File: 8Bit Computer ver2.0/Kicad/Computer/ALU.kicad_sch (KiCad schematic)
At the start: 36 parts, among them IC11 SN74HCS4075DR, IC12 SN74HCS4075DR, IC7 SN74LVC1G32DBVR, IC8 SN74LVC1G32DBVR

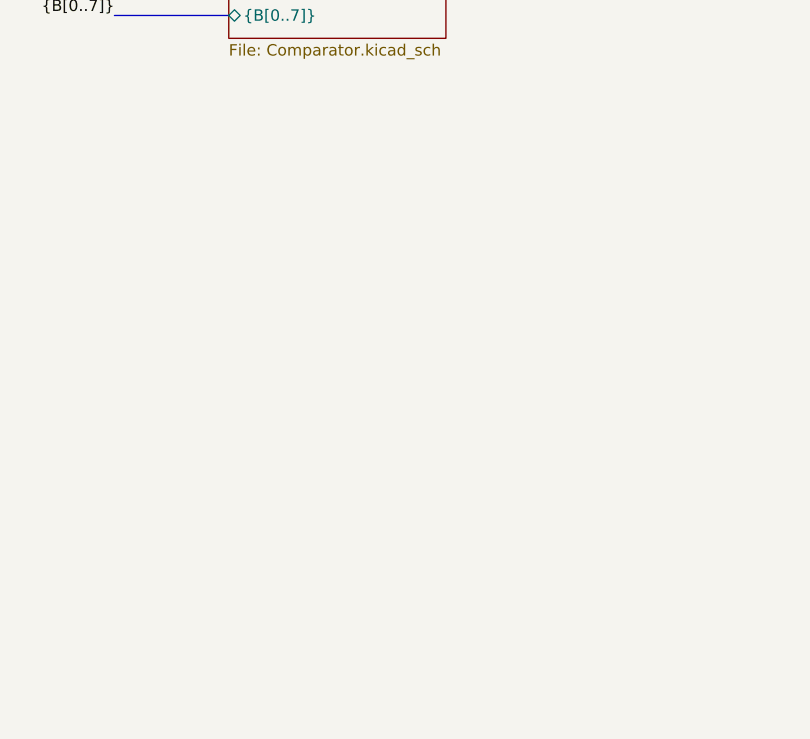
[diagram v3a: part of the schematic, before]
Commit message: parts, Kicad
parts:
added MUX 157 for BarrelShiftReg
Kicad:
began with BarrelShiftRegister
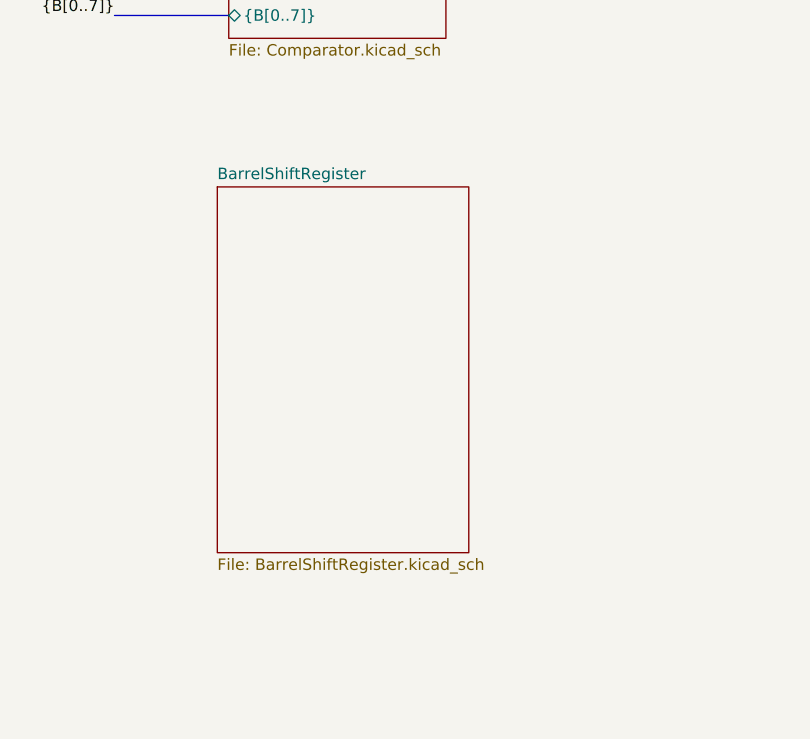
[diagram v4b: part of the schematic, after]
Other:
- added sheet BarrelShiftRegister (BarrelShiftRegister.kicad_sch)
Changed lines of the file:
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@@
+	)
+	(sheet
+		(at 466.09 354.33)
+		(size 27.94 40.64)
+		(exclude_from_sim no)
+		(in_bom yes)
+		(on_board yes)
+		(dnp no)
+		(fields_autoplaced yes)
+		(stroke
+			(width 0.1524)
+			(type solid)
+		)
+		(fill
+			(color 0 0 0 0.0000)
+		)
+		(property "Sheetname" "BarrelShiftRegister"
+			(at 466.09 353.6184 0)
+			(effects
+				(font
+					(size 1.27 1.27)
+				)
+				(justify left bottom)
+			)
+		)
+		(property "Sheetfile" "BarrelShiftRegister.kicad_sch"
+			(at 466.09 395.5546 0)
+			(effects
+				(font
+					(size 1.27 1.27)
+				)
+				(justify left top)
+			)
+		)
+		(instances
+			(project "Computer"
+				(path "/1196a00e-6878-4d6d-82b7-9e052dfe7c14/c4d8b530-1c6d-45af-88d2-7dc1d4321a34"
+					(page "15")
+				)
+			)
+		)
 	)
 	(sheet

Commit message: partsList, Kicad
parts:
added faster Comparator 521
added 1CH XOR
added 8Bit and 16Bit Driver 245, 16245
->they need pullUp resistors for High-Z when power on
Kicad:
included SRAM CAD Model AS7C1024
included some CAD Models
added Register 1 0x20 and 0x21
finished Incrementor
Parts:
- added C33, C34, C35, C36, C37, C38, C39, C40, C41, C42, C43, C44, C45, C46, C47, C48, C49, C50, C51, C52, C53, C54, C55, C56, C57, C58, C59, C60, C61, C62, C63, C64, C65, C66, C67, C68, C69, C70, C71, C72, C73, C74, C75, C76, C77, C78, C79, C80, C81, C82, C83, C84, C85, C86, C87, C88, C89, C90, C91, C92, C93, C94, C95, C96: 100nF, Capacitor_SMD:C_1206_3216Metric_Pad1.33x1.80mm_HandSolder, symbol Device:C
- added IC85: SN74ABT245BDWR, Samacsys:SOIC127P1030X265-20N, symbol Samacsys:SN74ABT245BDWR
- added IC86: SN74ABT574ADWR, Samacsys:SOIC127P1030X265-20N, symbol Samacsys:SN74ABT574ADWR
- added IC89: SN74LVC1G08DBVR, Samacsys:SOT95P280X145-5N, symbol Samacsys:SN74LVC1G08DBVR
- added IC90: SN74AHC74DR, Samacsys:SOIC127P600X175-14N, symbol Samacsys:SN74AHC74DR
- added IC91, IC94, IC95: SN74LVC1G14DBVR, Samacsys:SOT95P280X145-5N, symbol Samacsys:SN74LVC1G14DBVR
- added IC92, IC93: SN74F521DWR, Samacsys:SOIC127P1030X265-20N, symbol Samacsys:SN74F521DWR
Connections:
- net A0: now also IC85.2 (A1), IC86.19 (1Q)
- net A1: now also IC85.3 (A2), IC86.18 (2Q)
- net A2: now also IC85.4 (A3), IC86.17 (3Q)
- net A3: now also IC85.5 (A4), IC86.16 (4Q)
- net A4: now also IC85.6 (A5), IC86.15 (5Q)
- net A5: now also IC85.7 (A6), IC86.14 (6Q)
- net A6: now also IC85.8 (A7), IC86.13 (7Q)
- net A7: now also IC85.9 (A8), IC86.12 (8Q)
- net GND: now also C33.1, C34.1, C35.1, C36.1, C37.1, C38.1, C39.1, C40.1, C41.1, C42.1, C43.1, C44.1, C45.1, C46.1, C47.1, C48.1, C49.1, C50.1, C51.1, C52.1, C53.1, C54.1, C55.1, C56.1, C57.1, C58.1, C59.1, C60.1, C61.1, C62.1, C63.1, C64.1, C65.1, C66.1, C67.1, C68.1, C69.1, C70.1, C71.1, C72.1, C73.1, C74.1, C75.1, C76.1, C77.1, C78.1, C79.1, C80.1, C81.1, C82.1, C83.1, C84.1, C85.1, C86.1, C87.1, C88.1, C89.1, C90.1, C91.1, C92.1, C93.1, C94.1, C95.1, C96.1, IC85.10 (GND), IC86.1 (~{OE}), IC86.10 (GND), IC89.3 (GND), IC90.7 (GND), IC91.3 (GND), IC92.1 (~{OE}), IC92.10 (GND), IC93.1 (~{OE}), IC93.10 (GND), IC94.3 (GND), IC95.3 (GND)
- net VCC: now also C33.2, C34.2, C35.2, C36.2, C37.2, C38.2, C39.2, C40.2, C41.2, C42.2, C43.2, C44.2, C45.2, C46.2, C47.2, C48.2, C49.2, C50.2, C51.2, C52.2, C53.2, C54.2, C55.2, C56.2, C57.2, C58.2, C59.2, C60.2, C61.2, C62.2, C63.2, C64.2, C65.2, C66.2, C67.2, C68.2, C69.2, C70.2, C71.2, C72.2, C73.2, C74.2, C75.2, C76.2, C77.2, C78.2, C79.2, C80.2, C81.2, C82.2, C83.2, C84.2, C85.2, C86.2, C87.2, C88.2, C89.2, C90.2, C91.2, C92.2, C93.2, C94.2, C95.2, C96.2, IC85.1 (DIR), IC85.20 (VCC), IC86.20 (VCC), IC89.5 (VCC), IC90.1 (1~{CLR}), IC90.10 (2~{PRE}), IC90.11 (2CLK), IC90.12 (2D), IC90.13 (2~{CLR}), IC90.14 (VCC), IC90.4 (1~{PRE}), IC91.5 (VCC), IC92.20 (VCC), IC93.20 (VCC), IC94.5 (VCC), IC95.5 (VCC)
- net ~{CLK}: now also IC89.2 (B), IC91.2 (A)
- new net: IC92.19 (~{P_=_Q}), IC95.2 (A)
- new net: IC89.1 (A), IC95.4 (Y)
- new net: IC86.11 (CLK), IC89.4 (Y)
- new net: IC90.2 (1D), IC94.4 (Y)
- new net: IC90.3 (1CLK), IC91.4 (Y)
- new net: IC85.19 (~{OE}), IC90.6 (1~{Q})
- new net: IC93.19 (~{P_=_Q}), IC94.2 (A)
- new net CMD0: IC92.2 (P0), IC93.2 (P0)
- new net CMD1: IC92.4 (P1), IC93.4 (P1)
- new net CMD2: IC92.6 (P2), IC93.6 (P2)
- new net CMD3: IC92.8 (P3), IC93.8 (P3)
- new net CMD4: IC92.11 (P4), IC93.11 (P4)
- new net CMD5: IC92.13 (P5), IC93.13 (P5)
- new net CMD6: IC92.15 (P6), IC93.15 (P6)
- new net CMD7: IC92.17 (P7), IC93.17 (P7)
- new net DAT0: IC86.2 (1D)
- new net DAT1: IC86.3 (2D)
- new net DAT2: IC86.4 (3D)
- new net DAT3: IC86.5 (4D)
- new net DAT4: IC86.6 (5D)
- new net DAT5: IC86.7 (6D)
- new net DAT6: IC86.8 (7D)
- new net DAT7: IC86.9 (8D)
- new net Q0: IC85.18 (B1)
- new net Q1: IC85.17 (B2)
- new net Q2: IC85.16 (B3)
- new net Q3: IC85.15 (B4)
- new net Q4: IC85.14 (B5)
- new net Q5: IC85.13 (B6)
- new net Q6: IC85.12 (B7)
- new net Q7: IC85.11 (B8)
- no-connect marks 0 -> 3
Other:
- sheet BarrelShiftRegister ports: added DIS[0..7], GND, Q, STC, STF, VCC, {A[0..7]}, ~{CLK}; removed none
- sheet Incrementor ports: added Q[0..7], {C[0..7]}; removed C, Q
- note added: "0x20"
- note added: "0x21"
- note added: "REGISTER1"

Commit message: Kicad
added Register 2(0x22 u 0x23) and 3(0x13 u 0x14)
added BarrelShiftRegister
added AdderSubstractor
added cmd Comparators to the bitwise and binary Logic
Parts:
- added C100, C101, C102, C103, C104, C105, C106, C107, C108, C109, C110, C111, C112, C113, C114, C115, C116, C117, C118, C119, C120, C97, C98, C99: 100nF, Capacitor_SMD:C_1206_3216Metric_Pad1.33x1.80mm_HandSolder, symbol Device:C
- added IC100, IC107, IC108, IC109, IC125, IC126, IC128, IC130, IC132, IC134, IC136, IC138, IC98, IC99: SN74LVC1G14DBVR, Samacsys:SOT95P280X145-5N, symbol Samacsys:SN74LVC1G14DBVR
- added IC101, IC110: SN74ABT574ADWR, Samacsys:SOIC127P1030X265-20N, symbol Samacsys:SN74ABT574ADWR
- added IC102, IC111: SN74AHC74DR, Samacsys:SOIC127P600X175-14N, symbol Samacsys:SN74AHC74DR
- added IC103, IC112: SN74LVC1G08DBVR, Samacsys:SOT95P280X145-5N, symbol Samacsys:SN74LVC1G08DBVR
- added IC104, IC113: SN74ABT245BDWR, Samacsys:SOIC127P1030X265-20N, symbol Samacsys:SN74ABT245BDWR
- added IC105, IC106, IC123, IC124, IC127, IC129, IC131, IC133, IC135, IC137, IC96, IC97: SN74F521DWR, Samacsys:SOIC127P1030X265-20N, symbol Samacsys:SN74F521DWR
- added IC114: SN74LVC1G32DBVR, Samacsys:SOT95P280X145-5N, symbol Samacsys:SN74LVC1G32DBVR
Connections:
- net B0: now also IC101.19 (1Q), IC104.2 (A1)
- net B1: now also IC101.18 (2Q), IC104.3 (A2)
- net B2: now also IC101.17 (3Q), IC104.4 (A3)
- net B3: now also IC101.16 (4Q), IC104.5 (A4)
- net B4: now also IC101.15 (5Q), IC104.6 (A5)
- net B5: now also IC101.14 (6Q), IC104.7 (A6)
- net B6: now also IC101.13 (7Q), IC104.8 (A7)
- net B7: now also IC101.12 (8Q), IC104.9 (A8)
- net BinaryAND/EN: now also IC128.4 (Y)
- net BinaryNOT/EN: now also IC132.4 (Y)
- net BinaryOR/EN: now also IC130.4 (Y)
- net BinaryXOR/EN: now also IC125.4 (Y)
- net BitwiseAND/EN: now also IC136.4 (Y)
- net BitwiseNOT/EN: now also IC126.4 (Y)
- net BitwiseOR/EN: now also IC134.4 (Y)
- net BitwiseXOR/EN: now also IC138.4 (Y)
- net CMD0: now also IC105.2 (P0), IC106.2 (P0), IC123.2 (P0), IC124.2 (P0), IC127.2 (P0), IC129.2 (P0), IC131.2 (P0), IC133.2 (P0), IC135.2 (P0), IC137.2 (P0), IC96.2 (P0), IC97.2 (P0)
- net CMD1: now also IC105.4 (P1), IC106.4 (P1), IC123.4 (P1), IC124.4 (P1), IC127.4 (P1), IC129.4 (P1), IC131.4 (P1), IC133.4 (P1), IC135.4 (P1), IC137.4 (P1), IC96.4 (P1), IC97.4 (P1)
- net CMD2: now also IC105.6 (P2), IC106.6 (P2), IC123.6 (P2), IC124.6 (P2), IC127.6 (P2), IC129.6 (P2), IC131.6 (P2), IC133.6 (P2), IC135.6 (P2), IC137.6 (P2), IC96.6 (P2), IC97.6 (P2)
- net CMD3: now also IC105.8 (P3), IC106.8 (P3), IC123.8 (P3), IC124.8 (P3), IC127.8 (P3), IC129.8 (P3), IC131.8 (P3), IC133.8 (P3), IC135.8 (P3), IC137.8 (P3), IC96.8 (P3), IC97.8 (P3)
- net CMD4: now also IC105.11 (P4), IC106.11 (P4), IC123.11 (P4), IC124.11 (P4), IC127.11 (P4), IC129.11 (P4), IC131.11 (P4), IC133.11 (P4), IC135.11 (P4), IC137.11 (P4), IC96.11 (P4), IC97.11 (P4)
- net CMD5: now also IC105.13 (P5), IC106.13 (P5), IC123.13 (P5), IC124.13 (P5), IC127.13 (P5), IC129.13 (P5), IC131.13 (P5), IC133.13 (P5), IC135.13 (P5), IC137.13 (P5), IC96.13 (P5), IC97.13 (P5)
- net CMD6: now also IC105.15 (P6), IC106.15 (P6), IC123.15 (P6), IC124.15 (P6), IC127.15 (P6), IC129.15 (P6), IC131.15 (P6), IC133.15 (P6), IC135.15 (P6), IC137.15 (P6), IC96.15 (P6), IC97.15 (P6)
- net CMD7: now also IC105.17 (P7), IC106.17 (P7), IC123.17 (P7), IC124.17 (P7), IC127.17 (P7), IC129.17 (P7), IC131.17 (P7), IC133.17 (P7), IC135.17 (P7), IC137.17 (P7), IC96.17 (P7), IC97.17 (P7)
- net DAT0: now also IC101.2 (1D), IC110.2 (1D)
- net DAT1: now also IC101.3 (2D), IC110.3 (2D)
- net DAT2: now also IC101.4 (3D), IC110.4 (3D)
- net DAT3: now also IC101.5 (4D), IC110.5 (4D)
- net DAT4: now also IC101.6 (5D), IC110.6 (5D)
- net DAT5: now also IC101.7 (6D), IC110.7 (6D)
- net DAT6: now also IC101.8 (7D), IC110.8 (7D)
- net DAT7: now also IC101.9 (8D), IC110.9 (8D)
- net GND: now also IC92.12 (Q4), IC92.16 (Q6), IC92.18 (Q7), IC92.3 (Q0), IC92.5 (Q1), IC92.7 (Q2), IC92.9 (Q3), IC93.12 (Q4), IC93.16 (Q6), IC93.18 (Q7), IC93.5 (Q1), IC93.7 (Q2), IC93.9 (Q3), C100.1, C101.1, C102.1, C103.1, C104.1, C105.1, C106.1, C107.1, C108.1, C109.1, C110.1, C111.1, C112.1, C113.1, C114.1, C115.1, C116.1, C117.1, C118.1, C119.1, C120.1, C97.1, C98.1, C99.1, IC100.3 (GND), IC101.1 (~{OE}), IC101.10 (GND), IC102.7 (GND), IC103.3 (GND), IC104.10 (GND), IC105.1 (~{OE}), IC105.10 (GND), IC105.14 (Q5), IC105.16 (Q6), IC105.18 (Q7), IC105.7 (Q2), IC105.9 (Q3), IC106.1 (~{OE}), IC106.10 (GND), IC106.14 (Q5), IC106.16 (Q6), IC106.18 (Q7), IC106.3 (Q0), IC106.5 (Q1), IC106.9 (Q3), IC107.3 (GND), IC108.3 (GND), IC109.3 (GND), IC110.1 (~{OE}), IC110.10 (GND), IC111.7 (GND), IC112.3 (GND), IC113.10 (GND), IC114.3 (GND), IC123.1 (~{OE}), IC123.10 (GND), IC123.14 (Q5), IC123.16 (Q6), IC123.18 (Q7), IC123.3 (Q0), IC123.5 (Q1), IC123.7 (Q2), IC124.1 (~{OE}), IC124.10 (GND), IC124.14 (Q5), IC124.16 (Q6), IC124.18 (Q7), IC124.5 (Q1), IC124.7 (Q2), IC125.3 (GND), IC126.3 (GND), IC127.1 (~{OE}), IC127.10 (GND), IC127.14 (Q5), IC127.16 (Q6), IC127.18 (Q7), IC127.9 (Q3), IC128.3 (GND), IC129.1 (~{OE}), IC129.10 (GND), IC129.14 (Q5), IC129.16 (Q6), IC129.18 (Q7), IC129.3 (Q0), IC129.9 (Q3), IC130.3 (GND), IC131.1 (~{OE}), IC131.10 (GND), IC131.14 (Q5), IC131.16 (Q6), IC131.18 (Q7), IC131.5 (Q1), IC131.9 (Q3), IC132.3 (GND), IC133.1 (~{OE}), IC133.10 (GND), IC133.14 (Q5), IC133.16 (Q6), IC133.18 (Q7), IC133.3 (Q0), IC133.7 (Q2), IC134.3 (GND), IC135.1 (~{OE}), IC135.10 (GND), IC135.14 (Q5), IC135.16 (Q6), IC135.18 (Q7), IC135.7 (Q2), IC136.3 (GND), IC137.1 (~{OE}), IC137.10 (GND), IC137.14 (Q5), IC137.16 (Q6), IC137.18 (Q7), IC137.3 (Q0), IC137.5 (Q1), IC138.3 (GND), IC96.1 (~{OE}), IC96.10 (GND), IC96.12 (Q4), IC96.16 (Q6), IC96.18 (Q7), IC96.3 (Q0), IC96.7 (Q2), IC96.9 (Q3), IC97.1 (~{OE}), IC97.10 (GND), IC97.12 (Q4), IC97.16 (Q6), IC97.18 (Q7), IC97.7 (Q2), IC97.9 (Q3), IC98.3 (GND), IC99.3 (GND)
- net Q0: now also IC104.18 (B1), IC113.18 (B1)
- net Q1: now also IC104.17 (B2), IC113.17 (B2)
- net Q2: now also IC104.16 (B3), IC113.16 (B3)
- net Q3: now also IC104.15 (B4), IC113.15 (B4)
- net Q4: now also IC104.14 (B5), IC113.14 (B5)
- net Q5: now also IC104.13 (B6), IC113.13 (B6)
- net Q6: now also IC104.12 (B7), IC113.12 (B7)
- net Q7: now also IC104.11 (B8), IC113.11 (B8)
- net VCC: now also IC92.14 (Q5), IC93.14 (Q5), IC93.3 (Q0), C100.2, C101.2, C102.2, C103.2, C104.2, C105.2, C106.2, C107.2, C108.2, C109.2, C110.2, C111.2, C112.2, C113.2, C114.2, C115.2, C116.2, C117.2, C118.2, C119.2, C120.2, C97.2, C98.2, C99.2, IC100.5 (VCC), IC101.20 (VCC), IC102.1 (1~{CLR}), IC102.10 (2~{PRE}), IC102.11 (2CLK), IC102.12 (2D), IC102.13 (2~{CLR}), IC102.14 (VCC), IC102.4 (1~{PRE}), IC103.5 (VCC), IC104.1 (DIR), IC104.20 (VCC), IC105.12 (Q4), IC105.20 (VCC), IC105.3 (Q0), IC105.5 (Q1), IC106.12 (Q4), IC106.20 (VCC), IC106.7 (Q2), IC107.5 (VCC), IC108.5 (VCC), IC109.5 (VCC), IC110.20 (VCC), IC111.1 (1~{CLR}), IC111.10 (2~{PRE}), IC111.11 (2CLK), IC111.12 (2D), IC111.13 (2~{CLR}), IC111.14 (VCC), IC111.4 (1~{PRE}), IC112.5 (VCC), IC113.1 (DIR), IC113.20 (VCC), IC114.5 (VCC), IC123.12 (Q4), IC123.20 (VCC), IC123.9 (Q3), IC124.12 (Q4), IC124.20 (VCC), IC124.3 (Q0), IC124.9 (Q3), IC125.5 (VCC), IC126.5 (VCC), IC127.12 (Q4), IC127.20 (VCC), IC127.3 (Q0), IC127.5 (Q1), IC127.7 (Q2), IC128.5 (VCC), IC129.12 (Q4), IC129.20 (VCC), IC129.5 (Q1), IC129.7 (Q2), IC130.5 (VCC), IC131.12 (Q4), IC131.20 (VCC), IC131.3 (Q0), IC131.7 (Q2), IC132.5 (VCC), IC133.12 (Q4), IC133.20 (VCC), IC133.5 (Q1), IC133.9 (Q3), IC134.5 (VCC), IC135.12 (Q4), IC135.20 (VCC), IC135.3 (Q0), IC135.5 (Q1), IC135.9 (Q3), IC136.5 (VCC), IC137.12 (Q4), IC137.20 (VCC), IC137.7 (Q2), IC137.9 (Q3), IC138.5 (VCC), IC96.14 (Q5), IC96.20 (VCC), IC96.5 (Q1), IC97.14 (Q5), IC97.20 (VCC), IC97.3 (Q0), IC97.5 (Q1), IC98.5 (VCC), IC99.5 (VCC)
- net ~{CLK}: now also IC100.2 (A), IC103.2 (B), IC109.2 (A), IC112.2 (B)
- new net: IC129.19 (~{P_=_Q}), IC130.2 (A)
- new net: IC108.4 (Y), IC111.2 (1D)
- new net: IC109.4 (Y), IC111.3 (1CLK)
- new net: IC111.6 (1~{Q}), IC113.19 (~{OE})
- new net: IC123.19 (~{P_=_Q}), IC125.2 (A)
- new net: IC102.6 (1~{Q}), IC104.19 (~{OE})
- new net: IC133.19 (~{P_=_Q}), IC134.2 (A)
- new net: IC127.19 (~{P_=_Q}), IC128.2 (A)
- new net: IC131.19 (~{P_=_Q}), IC132.2 (A)
- new net: IC110.11 (CLK), IC112.4 (Y)
- new net: IC135.19 (~{P_=_Q}), IC136.2 (A)
- new net: IC102.2 (1D), IC99.4 (Y)
- new net: IC100.4 (Y), IC102.3 (1CLK)
- new net: IC101.11 (CLK), IC103.4 (Y)
- new net: IC97.19 (~{P_=_Q}), IC99.2 (A)
- new net: IC112.1 (A), IC114.4 (Y)
- new net: IC124.19 (~{P_=_Q}), IC126.2 (A)
- new net: IC137.19 (~{P_=_Q}), IC138.2 (A)
- new net: IC105.19 (~{P_=_Q}), IC107.2 (A)
- new net: IC107.4 (Y), IC114.1 (A)
- new net: IC106.19 (~{P_=_Q}), IC108.2 (A)
- new net: IC96.19 (~{P_=_Q}), IC98.2 (A)
- new net: IC103.1 (A), IC98.4 (Y)
- new net C0: IC110.19 (1Q), IC113.2 (A1)
- new net C1: IC110.18 (2Q), IC113.3 (A2)
- new net C2: IC110.17 (3Q), IC113.4 (A3)
- new net C3: IC110.16 (4Q), IC113.5 (A4)
- new net C4: IC110.15 (5Q), IC113.6 (A5)
- new net C5: IC110.14 (6Q), IC113.7 (A6)
- new net C6: IC110.13 (7Q), IC113.8 (A7)
- new net C7: IC110.12 (8Q), IC113.9 (A8)
- new net Q_{S}: IC114.2 (B)
- no-connect marks 3 -> 9
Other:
- added sheet AdderSubstractor (AdderSubstractor.kicad_sch)
- sheet BarrelShiftRegister ports: added Q[0..7], SFC, SFT; removed Q, STC, STF
- sheet FlagRegister ports: added DAT[0..7], Q[0..7]; removed DAT, Q
- sheet Incrementor ports: added Q_{S}; removed Q_{s}
- note added: "00010011"
- note added: "00010100"
- note added: "00010101"
- note added: "00010110"
- note added: "00010111"
- note added: "00011000"
- note added: "00011001"
- note added: "00011010"
- note added: "00011011"
- note added: "00011100"
- note added: "00100000"
- note added: "00100001"
- note added: "00100010"
- note added: "00100011"
- note added: "0x13"
- note added: "0x14"
- note added: "0x15"
- note added: "0x16"
- note added: "0x17"
- note added: "0x18"
- note added: "0x19"
- note added: "0x1A"
- note added: "0x1B"
- note added: "0x1C"
- note added: "0x22"
- note added: "0x23"
- note added: "REGISTER2"
- note added: "REGISTER3"
- moved on the sheet: C1, C10, C11, C12, C13, C14, C15, C16, C17, C18, C19, C2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

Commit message: Kicad
changed the comp values to the new ones
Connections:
- net GND: now also IC105.12 (Q4), IC105.3 (Q0), IC105.5 (Q1), IC106.12 (Q4), IC106.7 (Q2), IC123.9 (Q3), IC124.9 (Q3), IC127.7 (Q2), IC129.7 (Q2), IC131.7 (Q2), IC133.9 (Q3), IC135.9 (Q3), IC137.7 (Q2), IC92.14 (Q5), IC93.14 (Q5), IC97.14 (Q5); no longer IC105.14 (Q5), IC106.14 (Q5), IC106.3 (Q0), IC123.7 (Q2), IC124.7 (Q2), IC133.7 (Q2), IC135.7 (Q2), IC92.12 (Q4), IC92.7 (Q2), IC92.9 (Q3), IC93.12 (Q4), IC93.7 (Q2), IC93.9 (Q3), IC97.12 (Q4), IC97.7 (Q2), IC97.9 (Q3)
- net VCC: now also IC105.14 (Q5), IC106.14 (Q5), IC106.3 (Q0), IC123.7 (Q2), IC124.7 (Q2), IC133.7 (Q2), IC135.7 (Q2), IC92.12 (Q4), IC92.7 (Q2), IC92.9 (Q3), IC93.12 (Q4), IC93.7 (Q2), IC93.9 (Q3), IC97.12 (Q4), IC97.7 (Q2), IC97.9 (Q3); no longer IC105.12 (Q4), IC105.3 (Q0), IC105.5 (Q1), IC106.12 (Q4), IC106.7 (Q2), IC123.9 (Q3), IC124.9 (Q3), IC127.7 (Q2), IC129.7 (Q2), IC131.7 (Q2), IC133.9 (Q3), IC135.9 (Q3), IC137.7 (Q2), IC92.14 (Q5), IC93.14 (Q5), IC97.14 (Q5)
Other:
- note added: "0001 0001"
- note added: "0001 0010"
- note added: "0001 0011"
- note added: "0001 0100"
- note added: "0001 0101"
- note added: "0001 0110"
- note added: "0001 0111"
- note added: "0001 1000"
- note added: "00011101"
- note added: "00011110"
- note added: "00011111"
- note added: "0x11"
- note added: "0x12"
- note added: "0x1D"
- note added: "0x1E"
- note added: "0x1F"
- note removed: "00010011"
- note removed: "00010100"
- note removed: "00010101"
- note removed: "00010110"
- note removed: "00010111"
- note removed: "00011000"
- note removed: "00011001"
- note removed: "00011010"
- note removed: "00011011"
- note removed: "00100010"
- note removed: "00100011"
- note removed: "0x19"
- note removed: "0x1A"
- note removed: "0x1B"
- note removed: "0x22"
- note removed: "0x23"

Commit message: Kicad
deleted the Qs
began with FlashMemory
added the CMD comparators for Inc, Comp, AddSub, FlagReg, BarrelShifter, ProgCount
added Diodes and DATdis line
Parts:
- removed IC114: SN74LVC1G32DBVR, Samacsys:SOT95P280X145-5N, symbol Samacsys:SN74LVC1G32DBVR
- added D1, D10, D11, D12, D13, D14, D15, D16, D17, D18, D19, D2, D20, D21, D22, D23, D24, D25, D3, D4, D5, D6, D7, D8, D9: 1N4148, Diode_THT:D_DO-35_SOD27_P10.16mm_Horizontal, symbol Diode:1N4148
- added IC114, IC162, IC163, IC164, IC165, IC166, IC167, IC170, IC171, IC175, IC176, IC177, IC180, IC181: SN74LVC1G14DBVR, Samacsys:SOT95P280X145-5N, symbol Samacsys:SN74LVC1G14DBVR
- added IC155, IC156, IC157, IC158, IC159, IC160, IC161, IC168, IC169, IC172, IC173, IC174, IC178, IC179: SN74F521DWR, Samacsys:SOIC127P1030X265-20N, symbol Samacsys:SN74F521DWR
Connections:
- net AdderSubstractor/ADC: now also D6.2 (A), IC166.4 (Y)
- net AdderSubstractor/ADD: now also D5.2 (A), IC165.4 (Y)
- net AdderSubstractor/SUB: now also D7.2 (A), IC167.4 (Y)
- net BarrelShiftRegister/SFC: now also D14.2 (A), IC181.4 (Y)
- net BarrelShiftRegister/SFT: now also D13.2 (A), IC180.4 (Y)
- net BinaryAND/EN: now also D17.2 (A)
- net BinaryNOT/EN: now also D15.2 (A)
- net BinaryOR/EN: now also D16.2 (A)
- net BinaryXOR/EN: now also D18.2 (A)
- net BitwiseAND/EN: now also D21.2 (A)
- net BitwiseNOT/EN: now also D19.2 (A)
- net BitwiseOR/EN: now also D20.2 (A)
- net BitwiseXOR/EN: now also D22.2 (A)
- net CMD0: now also IC155.2 (P0), IC156.2 (P0), IC157.2 (P0), IC158.2 (P0), IC159.2 (P0), IC160.2 (P0), IC161.2 (P0), IC168.2 (P0), IC169.2 (P0), IC172.2 (P0), IC173.2 (P0), IC174.2 (P0), IC178.2 (P0), IC179.2 (P0)
- net CMD1: now also IC155.4 (P1), IC156.4 (P1), IC157.4 (P1), IC158.4 (P1), IC159.4 (P1), IC160.4 (P1), IC161.4 (P1), IC168.4 (P1), IC169.4 (P1), IC172.4 (P1), IC173.4 (P1), IC174.4 (P1), IC178.4 (P1), IC179.4 (P1)
- net CMD2: now also IC155.6 (P2), IC156.6 (P2), IC157.6 (P2), IC158.6 (P2), IC159.6 (P2), IC160.6 (P2), IC161.6 (P2), IC168.6 (P2), IC169.6 (P2), IC172.6 (P2), IC173.6 (P2), IC174.6 (P2), IC178.6 (P2), IC179.6 (P2)
- net CMD3: now also IC155.8 (P3), IC156.8 (P3), IC157.8 (P3), IC158.8 (P3), IC159.8 (P3), IC160.8 (P3), IC161.8 (P3), IC168.8 (P3), IC169.8 (P3), IC172.8 (P3), IC173.8 (P3), IC174.8 (P3), IC178.8 (P3), IC179.8 (P3)
- net CMD4: now also IC155.11 (P4), IC156.11 (P4), IC157.11 (P4), IC158.11 (P4), IC159.11 (P4), IC160.11 (P4), IC161.11 (P4), IC168.11 (P4), IC169.11 (P4), IC172.11 (P4), IC173.11 (P4), IC174.11 (P4), IC178.11 (P4), IC179.11 (P4)
- net CMD5: now also IC155.13 (P5), IC156.13 (P5), IC157.13 (P5), IC158.13 (P5), IC159.13 (P5), IC160.13 (P5), IC161.13 (P5), IC168.13 (P5), IC169.13 (P5), IC172.13 (P5), IC173.13 (P5), IC174.13 (P5), IC178.13 (P5), IC179.13 (P5)
- net CMD6: now also IC155.15 (P6), IC156.15 (P6), IC157.15 (P6), IC158.15 (P6), IC159.15 (P6), IC160.15 (P6), IC161.15 (P6), IC168.15 (P6), IC169.15 (P6), IC172.15 (P6), IC173.15 (P6), IC174.15 (P6), IC178.15 (P6), IC179.15 (P6)
- net CMD7: now also IC155.17 (P7), IC156.17 (P7), IC157.17 (P7), IC158.17 (P7), IC159.17 (P7), IC160.17 (P7), IC161.17 (P7), IC168.17 (P7), IC169.17 (P7), IC172.17 (P7), IC173.17 (P7), IC174.17 (P7), IC178.17 (P7), IC179.17 (P7)
- net CMP_{bigger}: now also D10.2 (A), IC175.4 (Y)
- net CMP_{equal}: now also D11.2 (A), IC176.4 (Y)
- net CMP_{smaller}: now also D12.2 (A), IC177.4 (Y)
- net GND: now also IC114.3 (GND), IC155.1 (~{OE}), IC155.10 (GND), IC155.12 (Q4), IC155.16 (Q6), IC155.18 (Q7), IC155.3 (Q0), IC155.7 (Q2), IC155.9 (Q3), IC156.1 (~{OE}), IC156.10 (GND), IC156.12 (Q4), IC156.16 (Q6), IC156.18 (Q7), IC156.7 (Q2), IC156.9 (Q3), IC157.1 (~{OE}), IC157.10 (GND), IC157.12 (Q4), IC157.16 (Q6), IC157.18 (Q7), IC157.3 (Q0), IC157.5 (Q1), IC157.9 (Q3), IC158.1 (~{OE}), IC158.10 (GND), IC158.14 (Q5), IC158.16 (Q6), IC158.18 (Q7), IC158.5 (Q1), IC158.9 (Q3), IC159.1 (~{OE}), IC159.10 (GND), IC159.12 (Q4), IC159.14 (Q5), IC159.16 (Q6), IC159.18 (Q7), IC159.3 (Q0), IC159.5 (Q1), IC160.1 (~{OE}), IC160.10 (GND), IC160.12 (Q4), IC160.14 (Q5), IC160.16 (Q6), IC160.18 (Q7), IC160.5 (Q1), IC161.1 (~{OE}), IC161.10 (GND), IC161.12 (Q4), IC161.14 (Q5), IC161.16 (Q6), IC161.18 (Q7), IC161.3 (Q0), IC162.3 (GND), IC163.3 (GND), IC164.3 (GND), IC165.3 (GND), IC166.3 (GND), IC167.3 (GND), IC168.1 (~{OE}), IC168.10 (GND), IC168.12 (Q4), IC168.14 (Q5), IC168.16 (Q6), IC168.18 (Q7), IC169.1 (~{OE}), IC169.10 (GND), IC169.14 (Q5), IC169.16 (Q6), IC169.18 (Q7), IC169.3 (Q0), IC169.5 (Q1), IC169.7 (Q2), IC169.9 (Q3), IC170.3 (GND), IC171.3 (GND), IC172.1 (~{OE}), IC172.10 (GND), IC172.14 (Q5), IC172.16 (Q6), IC172.18 (Q7), IC172.5 (Q1), IC172.7 (Q2), IC173.1 (~{OE}), IC173.10 (GND), IC173.14 (Q5), IC173.16 (Q6), IC173.18 (Q7), IC173.3 (Q0), IC173.7 (Q2), IC174.1 (~{OE}), IC174.10 (GND), IC174.14 (Q5), IC174.16 (Q6), IC174.18 (Q7), IC174.7 (Q2), IC175.3 (GND), IC176.3 (GND), IC177.3 (GND), IC178.1 (~{OE}), IC178.10 (GND), IC178.12 (Q4), IC178.16 (Q6), IC178.18 (Q7), IC178.3 (Q0), IC178.9 (Q3), IC179.1 (~{OE}), IC179.10 (GND), IC179.12 (Q4), IC179.16 (Q6), IC179.18 (Q7), IC179.9 (Q3), IC180.3 (GND), IC181.3 (GND)
- net Incrementor/DEC: now also D9.2 (A), IC171.4 (Y)
- net Incrementor/INC: now also D8.2 (A), IC170.4 (Y)
- net LDA: now also D1.2 (A), IC164.4 (Y)
- net LDC: now also D3.2 (A), IC162.4 (Y)
- net LDF: now also D2.2 (A), IC163.4 (Y)
- net STA: now also D4.2 (A), IC114.4 (Y)
- net VCC: now also IC114.5 (VCC), IC155.14 (Q5), IC155.20 (VCC), IC155.5 (Q1), IC156.14 (Q5), IC156.20 (VCC), IC156.3 (Q0), IC156.5 (Q1), IC157.14 (Q5), IC157.20 (VCC), IC157.7 (Q2), IC158.12 (Q4), IC158.20 (VCC), IC158.3 (Q0), IC158.7 (Q2), IC159.20 (VCC), IC159.7 (Q2), IC159.9 (Q3), IC160.20 (VCC), IC160.3 (Q0), IC160.7 (Q2), IC160.9 (Q3), IC161.20 (VCC), IC161.5 (Q1), IC161.7 (Q2), IC161.9 (Q3), IC162.5 (VCC), IC163.5 (VCC), IC164.5 (VCC), IC165.5 (VCC), IC166.5 (VCC), IC167.5 (VCC), IC168.20 (VCC), IC168.3 (Q0), IC168.5 (Q1), IC168.7 (Q2), IC168.9 (Q3), IC169.12 (Q4), IC169.20 (VCC), IC170.5 (VCC), IC171.5 (VCC), IC172.12 (Q4), IC172.20 (VCC), IC172.3 (Q0), IC172.9 (Q3), IC173.12 (Q4), IC173.20 (VCC), IC173.5 (Q1), IC173.9 (Q3), IC174.12 (Q4), IC174.20 (VCC), IC174.3 (Q0), IC174.5 (Q1), IC174.9 (Q3), IC175.5 (VCC), IC176.5 (VCC), IC177.5 (VCC), IC178.14 (Q5), IC178.20 (VCC), IC178.5 (Q1), IC178.7 (Q2), IC179.14 (Q5), IC179.20 (VCC), IC179.3 (Q0), IC179.5 (Q1), IC179.7 (Q2), IC180.5 (VCC), IC181.5 (VCC)
- net at IC108.4 (Y), IC111.2 (1D): now also D25.2 (A)
- net at IC90.2 (1D), IC94.4 (Y): now also D23.2 (A)
- net at IC102.2 (1D), IC99.4 (Y): now also D24.2 (A)
- net at IC112.1 (A): now also IC107.4 (Y)
- new net: IC114.2 (A), IC155.19 (~{P_=_Q})
- new net: IC174.19 (~{P_=_Q}), IC177.2 (A)
- new net: IC158.19 (~{P_=_Q}), IC164.2 (A)
- new net: IC168.19 (~{P_=_Q}), IC170.2 (A)
- new net: IC169.19 (~{P_=_Q}), IC171.2 (A)
- new net: IC179.19 (~{P_=_Q}), IC181.2 (A)
- new net: IC173.19 (~{P_=_Q}), IC176.2 (A)
- new net: IC178.19 (~{P_=_Q}), IC180.2 (A)
- new net: IC156.19 (~{P_=_Q}), IC162.2 (A)
- new net: IC172.19 (~{P_=_Q}), IC175.2 (A)
- new net: IC157.19 (~{P_=_Q}), IC163.2 (A)
- new net: IC161.19 (~{P_=_Q}), IC167.2 (A)
- new net: IC160.19 (~{P_=_Q}), IC166.2 (A)
- new net: IC159.19 (~{P_=_Q}), IC165.2 (A)
- new net DAT_{dis}: D1.1 (K), D10.1 (K), D11.1 (K), D12.1 (K), D13.1 (K), D14.1 (K), D15.1 (K), D16.1 (K), D17.1 (K), D18.1 (K), D19.1 (K), D2.1 (K), D20.1 (K), D21.1 (K), D22.1 (K), D23.1 (K), D24.1 (K), D25.1 (K), D3.1 (K), D4.1 (K), D5.1 (K), D6.1 (K), D7.1 (K), D8.1 (K), D9.1 (K)
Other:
- sheet Incrementor ports: added none; removed Q_{S}
- note added: "0000 1100"
- note added: "0000 1101"
- note added: "0000 1110"
- note added: "0000 1111"
- note added: "0001 0000"
- note added: "0001 1001"
- note added: "0001 1010"
- note added: "0001 1011"
- note added: "0010 0010"
- note added: "0010 0011"
- note added: "0010 0100"
- note added: "0010 0101"
- note added: "0010 0110"
- note added: "0010 0111"
- note added: "0x0C"
- note added: "0x0D"
- note added: "0x0E"
- note added: "0x0F"
- note added: "0x10"
- note added: "0x19"
- note added: "0x1A"
- note added: "0x1B"
- note added: "0x22"
- note added: "0x23"
- note added: "0x24"
- note added: "0x25"
- note added: "0x26"
- note added: "0x27"
- moved on the sheet: IC100, IC108, IC109, IC11, IC12, IC123, IC124, IC125, IC126, IC127, IC128, IC129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
